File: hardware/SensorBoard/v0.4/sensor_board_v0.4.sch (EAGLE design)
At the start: 59 parts, among them IC1 MCP1703CB, IC2 MCP1703CB, J3 USB-MICROB, Q1 MMBT5088-NPN, U1 ATMEGA328P, U2 TSL2561FN, U4 MPL115A, U5 FT231XS, Y1 16MHZ

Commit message: Minor touches
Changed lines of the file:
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@@
 <segment>
 <pinref part="U$4" gate="G$1" pin="ANT"/>
-<wire x1="93.98" y1="30.48" x2="101.6" y2="30.48" width="0.1524" layer="91"/>
+<wire x1="93.98" y1="30.48" x2="99.06" y2="30.48" width="0.1524" layer="91"/>
 <label x="101.6" y="30.48" size="1.778" layer="95" xref="yes"/>
+<wire x1="99.06" y1="30.48" x2="101.6" y2="30.48" width="0.1524" layer="91"/>
+<wire x1="99.06" y1="30.48" x2="99.06" y2="38.1" width="0.1524" layer="91"/>
+<wire x1="99.06" y1="38.1" x2="116.84" y2="38.1" width="0.1524" layer="91"/>
+<junction x="99.06" y="30.48"/>
 <pinref part="X1" gate="G$1" pin="ANT"/>
-<wire x1="116.84" y1="30.48" x2="116.84" y2="33.02" width="0.1524" layer="91"/>
-<wire x1="116.84" y1="33.02" x2="111.76" y2="38.1" width="0.1524" layer="91"/>
-<wire x1="111.76" y1="38.1" x2="101.6" y2="38.1" width="0.1524" layer="91"/>
-<wire x1="101.6" y1="38.1" x2="93.98" y2="30.48" width="0.1524" layer="91"/>
-<junction x="93.98" y="30.48"/>
+<wire x1="116.84" y1="38.1" x2="116.84" y2="30.48" width="0.1524" layer="91"/>
 </segment>
 </net>

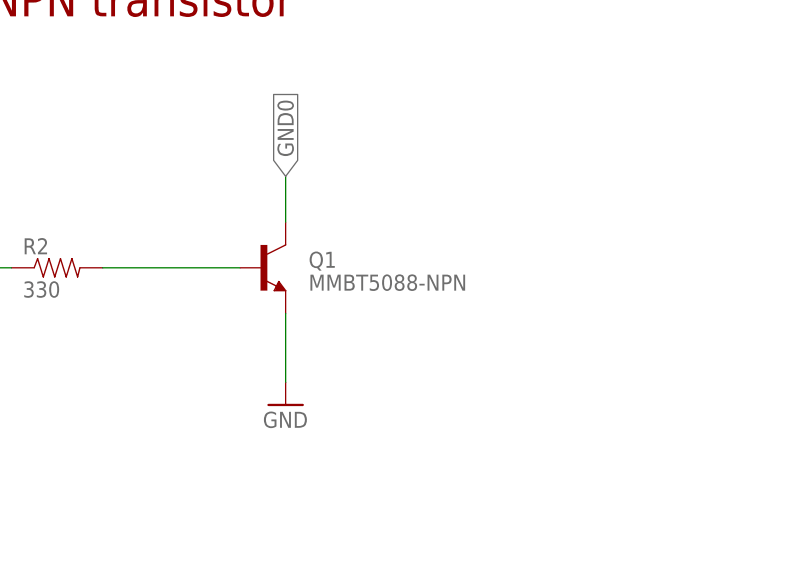
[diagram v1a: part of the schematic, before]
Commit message: Removed 'label' from SMA connector
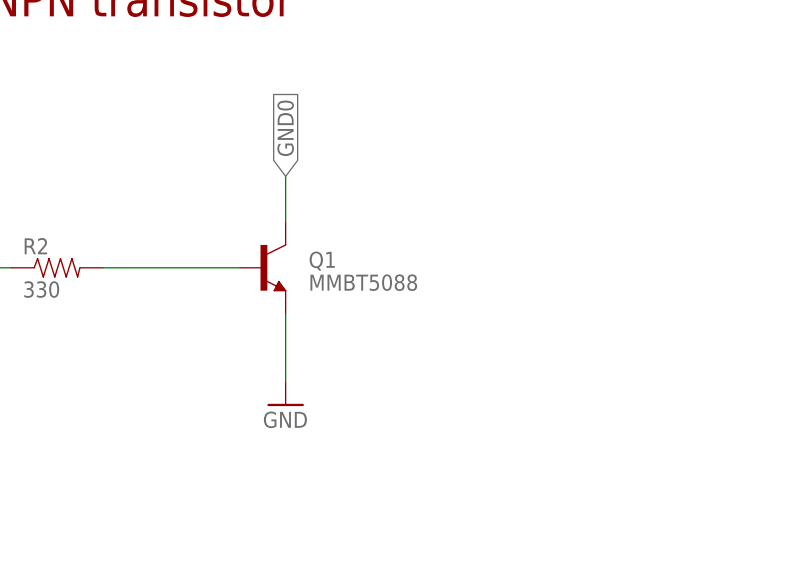
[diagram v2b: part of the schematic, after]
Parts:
- Q1: value MMBT5088-NPN -> MMBT5088
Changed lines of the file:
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@@
 <attribute name="OC_NEWARK" value="unknown"/>
 </part>
-<part name="Q1" library="SparkFun-DiscreteSemi" deviceset="TRANSISTOR_NPN" device="MMBT5088" value="MMBT5088-NPN">
+<part name="Q1" library="SparkFun-DiscreteSemi" deviceset="TRANSISTOR_NPN" device="MMBT5088" value="MMBT5088">
 <attribute name="MF" value=""/>
 <attribute name="MPN" value=""/>
